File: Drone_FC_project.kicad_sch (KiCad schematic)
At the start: 28 parts, among them J5 Conn_01x04_Pin, J6 USB_C_Receptacle, SW2 SW_Push, U3 AP2112K-3.3TRG1, U4 STM32F411CEU6, Y1 8MHz

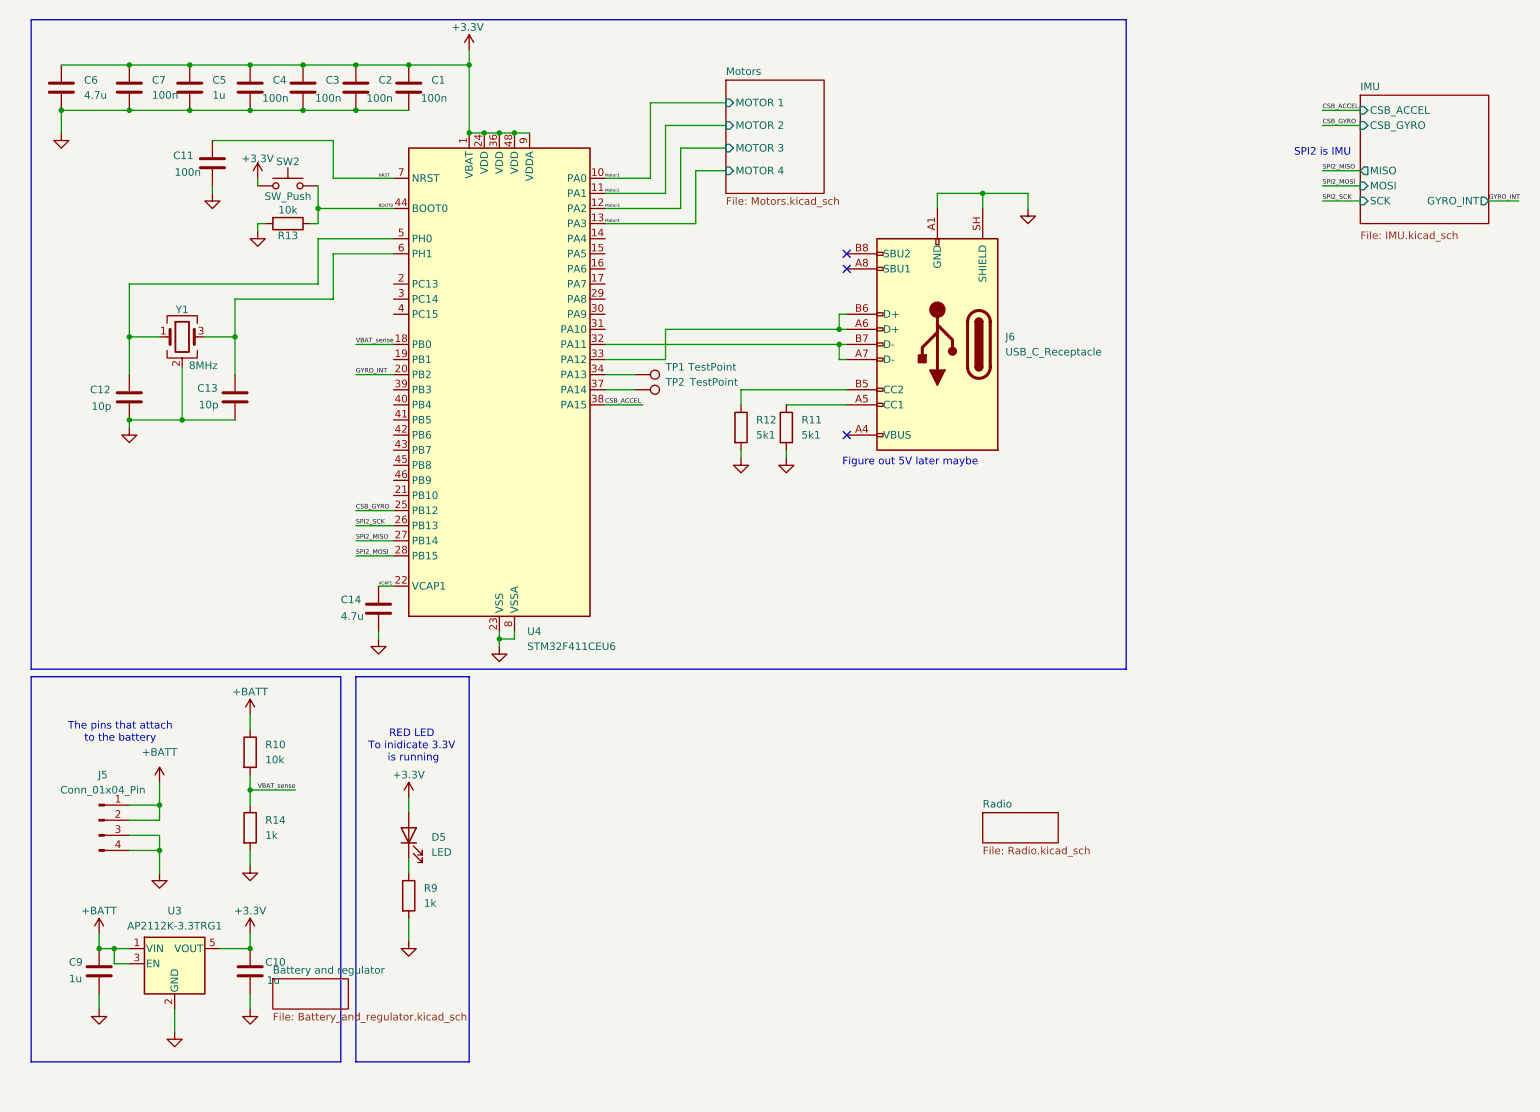
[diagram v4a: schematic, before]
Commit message: Created radio, cleanup a few other things
Finished radio schematic, added datasheets, added a stm32cubemx file for pinouts, added SPI1 and SPI2.
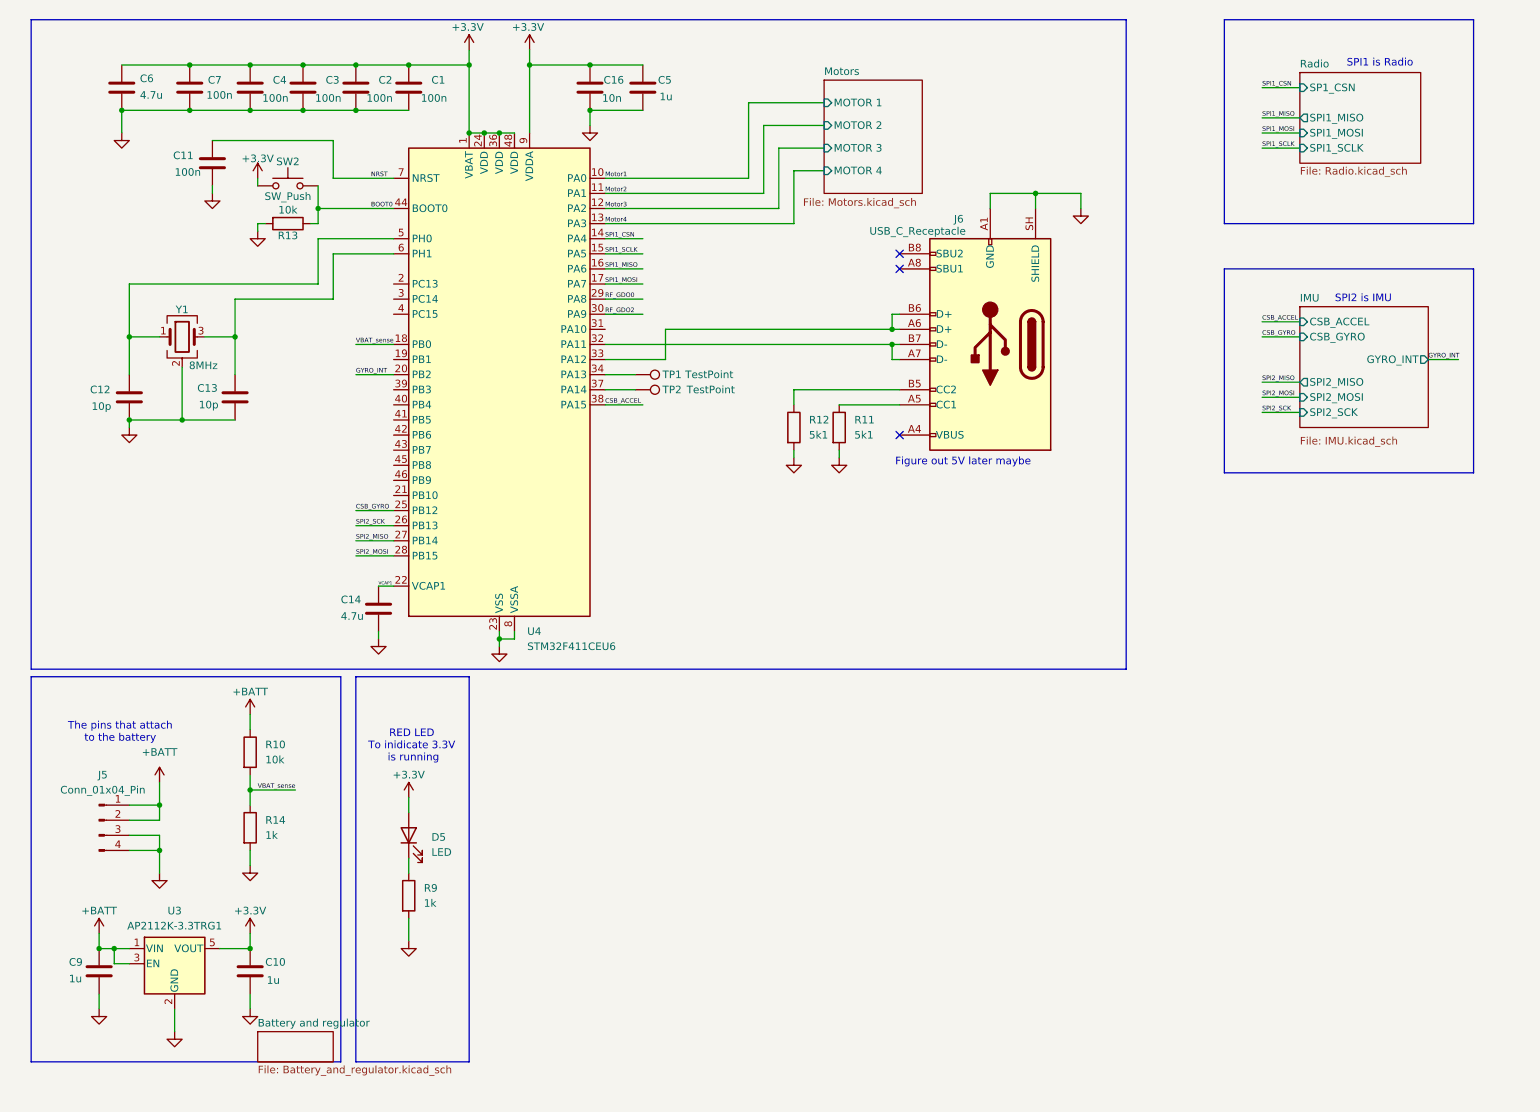
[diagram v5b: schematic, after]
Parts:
- added C16: 10n, Capacitor_SMD:C_0603_1608Metric, symbol Device:C
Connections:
- net +3.3V: now also C16.1
- net GND: now also C16.2
- net SPI1_CSN: now reaches U4.14 (PA4)
- net SPI1_SCLK: now reaches U4.15 (PA5)
- net SPI1_MISO: now reaches U4.16 (PA6)
- net SPI1_MOSI: now reaches U4.17 (PA7)
- net RF_GDO0: now reaches U4.29 (PA8)
- net RF_GDO2: now reaches U4.30 (PA9)
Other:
- sheet IMU ports: added SPI2_MISO, SPI2_MOSI, SPI2_SCK; removed MISO, MOSI, SCK
- sheet Radio ports: added SP1_CSN, SPI1_MISO, SPI1_MOSI, SPI1_SCLK; removed none
- note added: "SPI1 is Radio"
- moved on the sheet: C5, C6, C7, J6, R11, R12

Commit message: Fixing some radio things
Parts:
- added D6: LED, symbol Device:LED
- added R16: 1k, symbol Device:R
- C12, C13: value 10p -> 15p
- Y1: value 8MHz -> X322516MOB4SI
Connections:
- net +BATT: now also D6.2 (A)
- net GND: now also R16.2
- new net: D6.1 (K), R16.1
- no-connect marks 3 -> 16
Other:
- removed sheet Battery and regulator
- sheet Radio ports: added RF_GDO0, RF_GDO2; removed none
- note added: "2*(C_L-C_Stray)=15p"
- note added: "RED LED To inidicate BATT is connected"

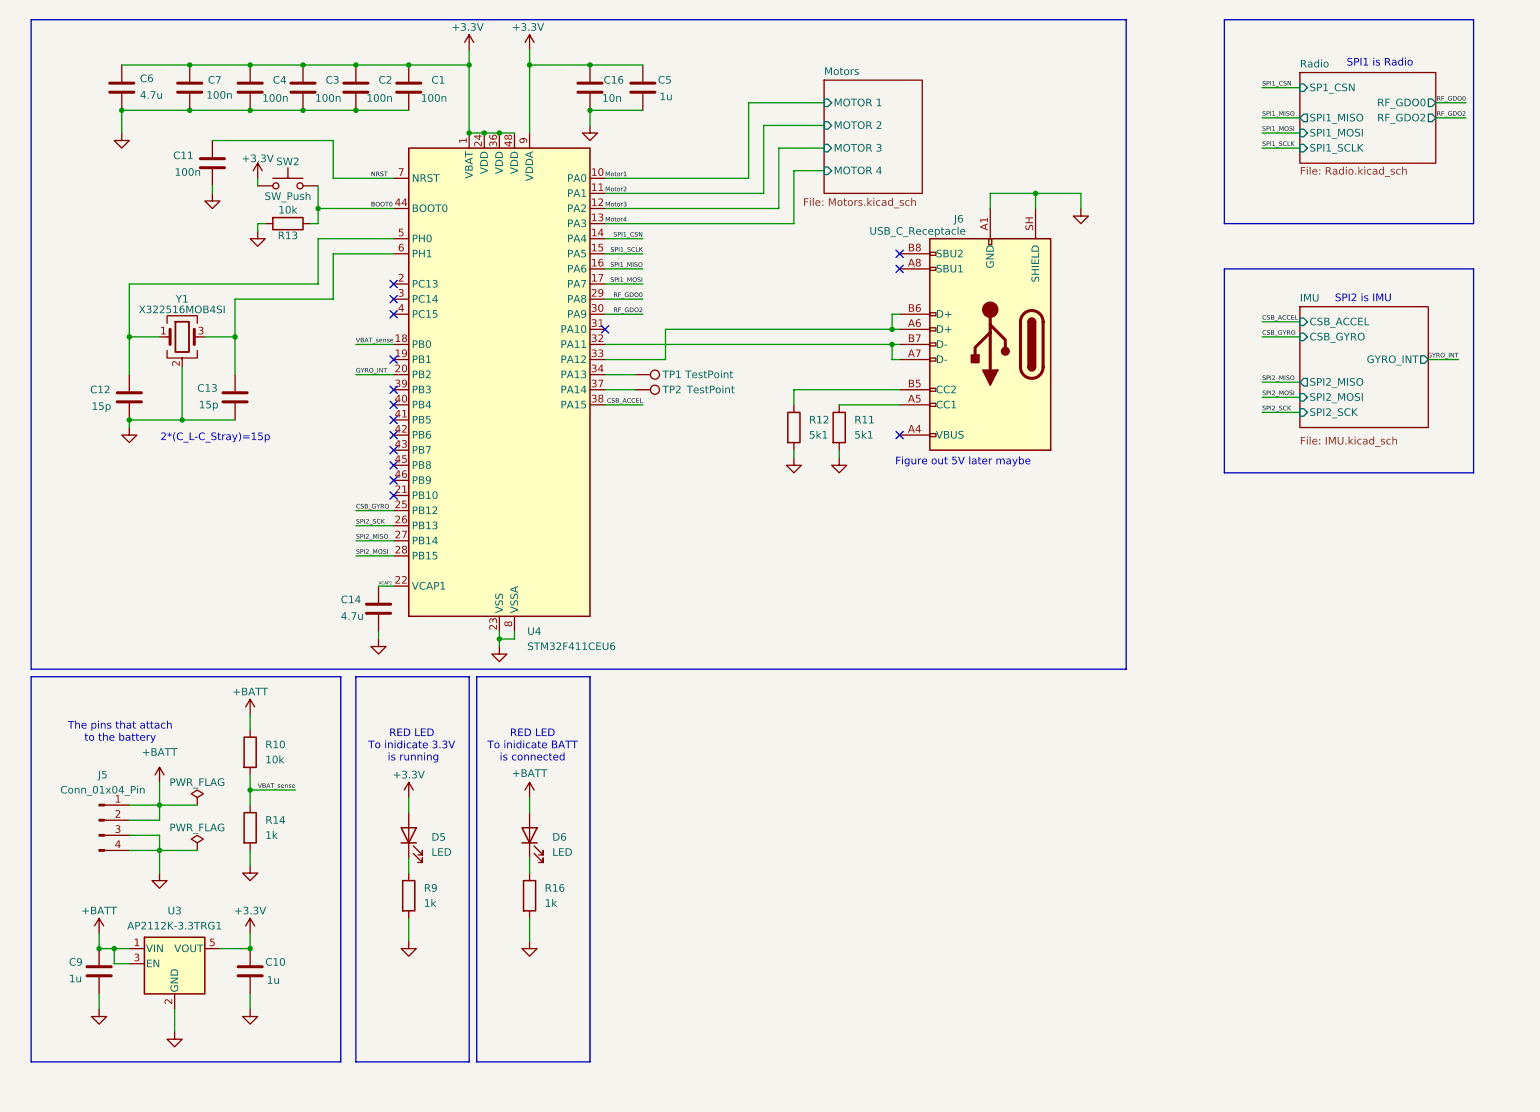
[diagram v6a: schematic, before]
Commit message: Motor and UBS 5V update
Motors each have a RED LED to indicate their on status.
5V on USB now runs when and only when the USB is plugged in. It will ignore battery otherwise. Green Led's indicate if the power is running.
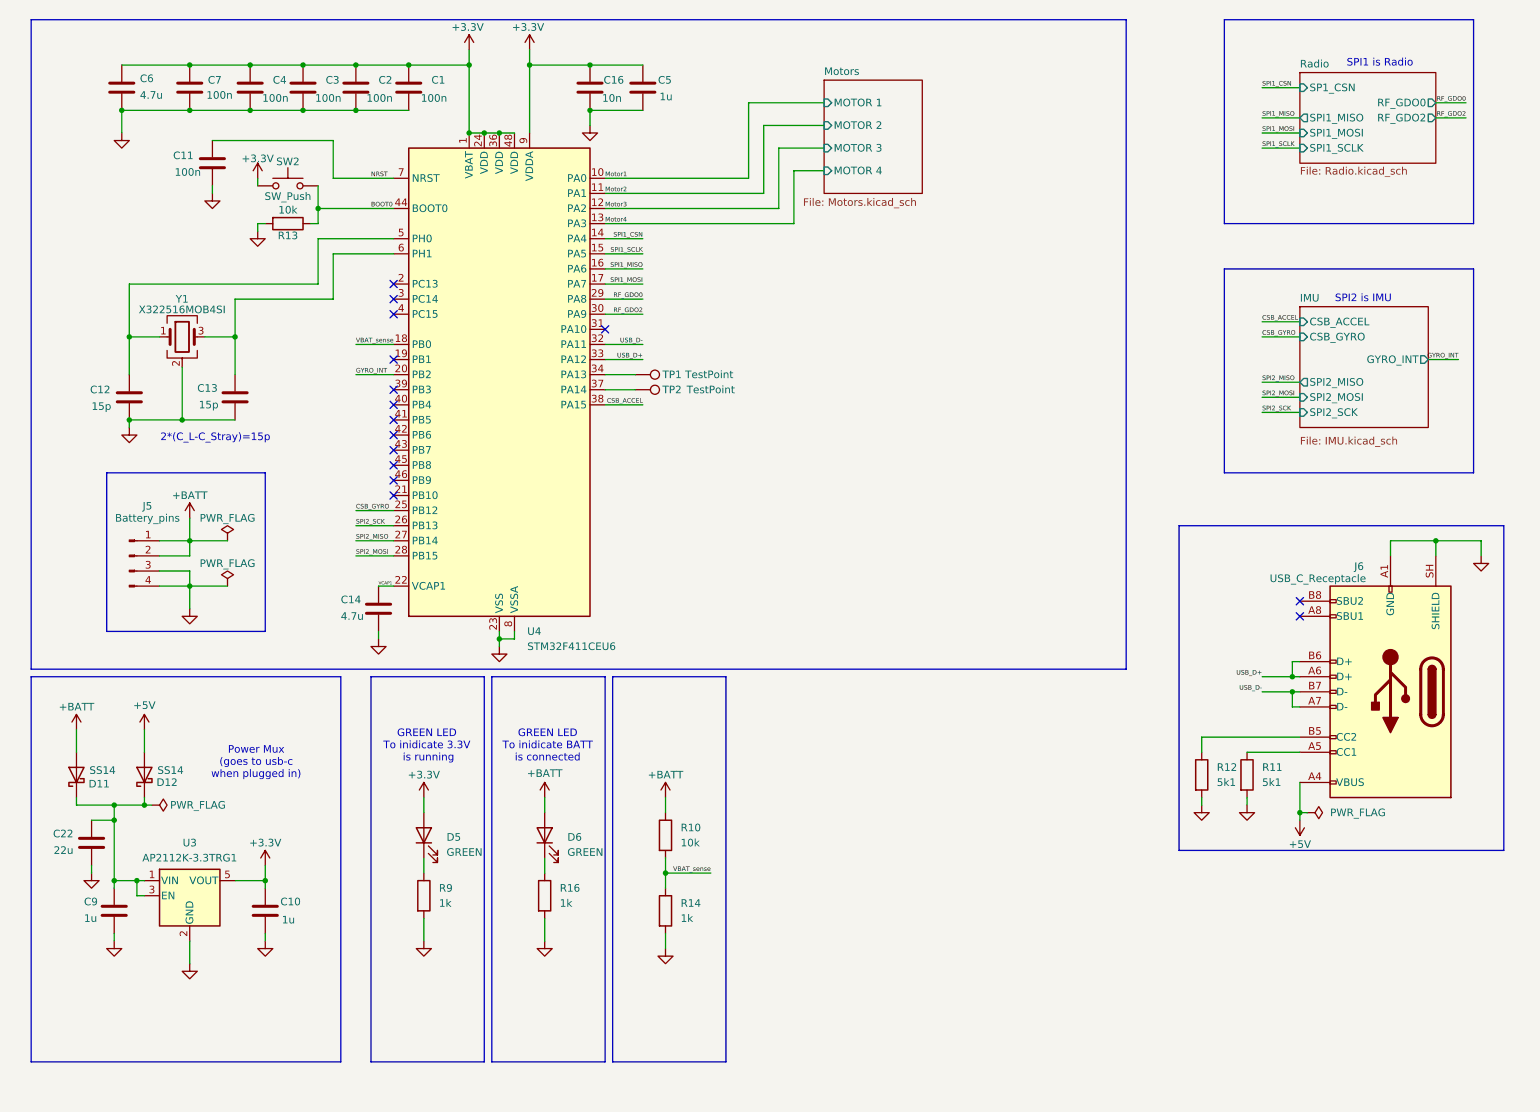
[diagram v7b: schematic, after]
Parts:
- added C22: 22u, Package_SO:SOIC-8_3.9x4.9mm_P1.27mm, symbol Device:C
- added D11, D12: SS14, Diode_SMD:D_SMA, symbol Diode:SS14
- D5, D6: value LED -> GREEN
- J5: value Conn_01x04_Pin -> Battery_pins
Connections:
- net +BATT: now also D11.2 (A); no longer C9.1, U3.1 (VIN), U3.3 (EN)
- net GND: now also C22.2
- net +5V: now reaches J6.A4 (VBUS), J6.A9 (VBUS), J6.B4 (VBUS), J6.B9 (VBUS)
- net +5V: now also D12.2 (A)
- net USB_D+: now reaches J6.A6 (D+), J6.B6 (D+), U4.33 (PA12)
- net USB_D-: now reaches J6.A7 (D-), J6.B7 (D-), U4.32 (PA11)
- new net: C22.1, C9.1, D11.1 (K), D12.1 (K), U3.1 (VIN), U3.3 (EN)
- no-connect marks 16 -> 15
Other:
- note added: "GREEN LED To inidicate 3.3V is running"
- note added: "GREEN LED To inidicate BATT is connected"
- note added: "Power Mux (goes to usb-c when plugged in)"
- note removed: "Figure out 5V later maybe"
- note removed: "RED LED To inidicate 3.3V is running"
- note removed: "RED LED To inidicate BATT is connected"
- note removed: "The pins that attach to the battery"
- moved on the sheet: C10, C9, D5, D6, J5, J6, R10, R11, R12, R14, R16, R9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
